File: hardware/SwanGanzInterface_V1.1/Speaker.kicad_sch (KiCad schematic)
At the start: 0 parts

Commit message: Added crystal loading caps
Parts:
- added C28: C, symbol Device:C
- added U15: OPA2350, Package_DIP:DIP-8_W7.62mm, symbol SGI_SymbolLib:OPA2350PA
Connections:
- new net: U15.1, U15.2 (-)
- new net +3V3: C28.1, U15.8 (V+)
- new net GND: C28.2, U15.4 (V-)

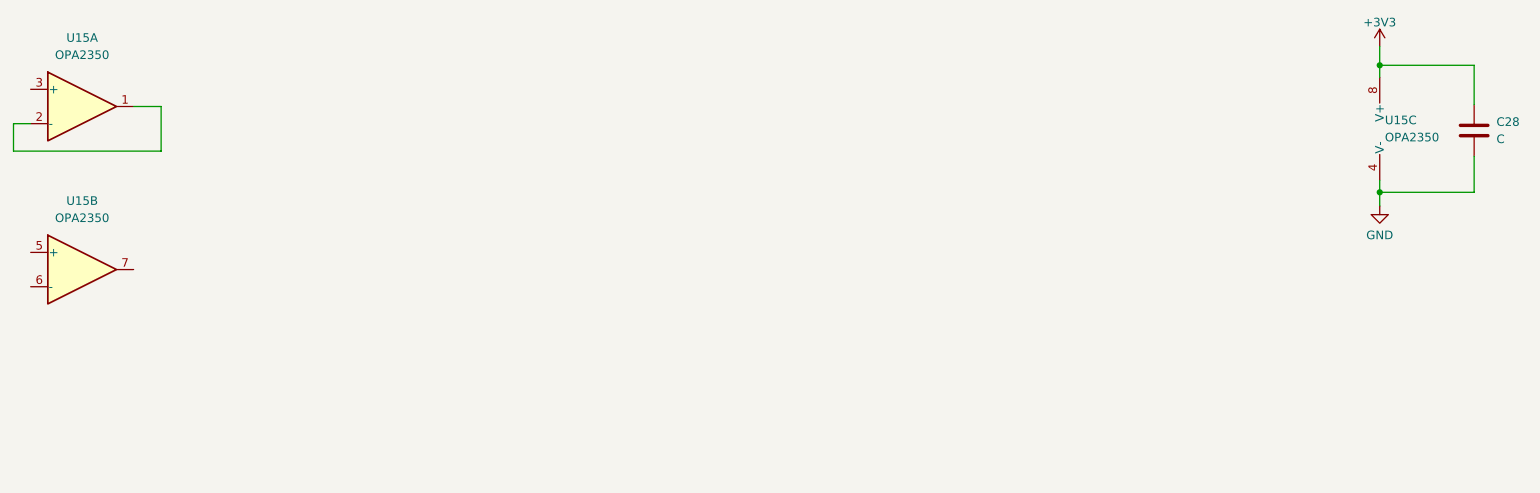
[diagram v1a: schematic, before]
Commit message: Added audio ampliier to symbol lib, began converting speaker circuit to audio amplifier
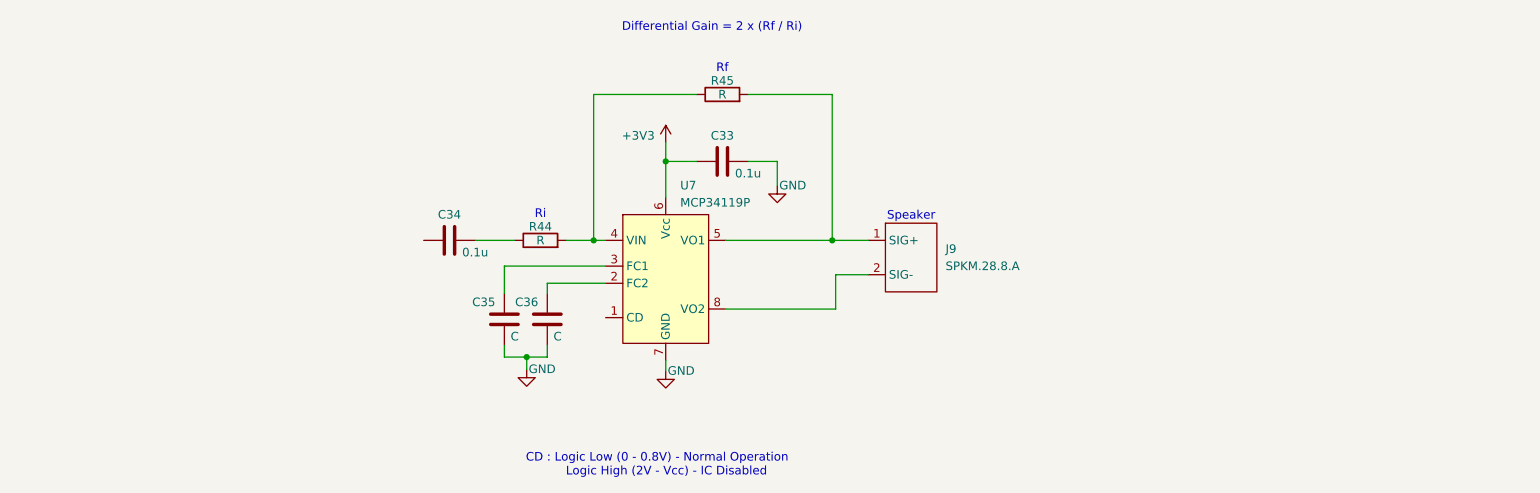
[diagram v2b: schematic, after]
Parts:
- removed C28: C, symbol Device:C
- removed U15: OPA2350, Package_DIP:DIP-8_W7.62mm, symbol SGI_SymbolLib:OPA2350PA
- added C33, C34: 0.1u, symbol Device:C
- added C35, C36: C, symbol Device:C
- added J9: SPKM.28.8.A, TerminalBlock:TerminalBlock_MaiXu_MX126-5.0-02P_1x02_P5.00mm, symbol SGI_SymbolLib:SPKM.28.8.A
- added R44, R45: R, symbol Device:R
- added U7: MCP34119P, Package_DIP:DIP-8_W7.62mm_LongPads, symbol SGI_SymbolLib:MCP34119P
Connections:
- net +3V3: now also C33.1, U7.6 (Vcc)
- net GND: now also C33.2, C35.1, C36.1, U7.7 (GND)
- new net: C34.2, R44.1
- new net: R44.2, R45.1, U7.4 (VIN)
- new net: C36.2, U7.2 (FC2)
- new net: J9.1 (SIG+), R45.2, U7.5 (VO1)
- new net: J9.2 (SIG-), U7.8 (VO2)
- new net: C35.2, U7.3 (FC1)
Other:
- note added: "CD : Logic Low (0 - 0.8V) - Normal Operation Logic High (2V - Vcc) - IC Disabled"
- note added: "Differential Gain = 2 x (Rf / Ri)"
- note added: "Rf"
- note added: "Ri"
- note added: "Speaker"

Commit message: Calculated speaker gain
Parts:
- R44: value R -> 16.6k
- R45: value R -> 10k
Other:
- note added: "DAC Range : 0 to 3.3V Gain = 1 / 3.3 = ~0.3 Differential Gain = 2 x (Rf / Ri) 0.3 = 2 x (Rf / Ri) 0.6 = Rf / Ri Ri = Rf / 0.6 Let Rf = 10 kOhms Ri = 10k / 0.6 Ri = 16.67 kOhms Rf = 10k kOhms Ri = 16.67 kOhms"
- note added: "P = V^2 / R 1W = V^2 / 8 V^2 = 8 V = 2.83 Vrms 2.83 Vrms = Vpp / (2 * sqrt(2)) Vpp = 1V"
- note added: "Speaker: Input Impedance : 8 Ohms Frequency Range : 100 Hz - 10kHz Nominal Power Input : 1 Watt RMS Maximum Power Input : 1.5 Watts"
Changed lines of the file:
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@@
+		)
+	)
+	(text "P = V^2 / R\n1W = V^2 / 8\nV^2 = 8\nV = 2.83 Vrms \n2.83 Vrms = Vpp / (2 * sqrt(2))\nVpp = 1V"
+		(exclude_from_sim no)
+		(at 227.33 64.77 0)
+		(effects
+			(font
+				(size 1.27 1.27)
+			)
+		)
+	)
+	(text "Speaker:\nInput Impedance : 8 Ohms\nFrequency Range : 100 Hz - 10kHz\nNominal Power Input : 1 Watt RMS\nMaximum Power Input : 1.5 Watts"
+		(exclude_from_sim no)
+		(at 226.568 46.228 0)
+		(effects
+			(font
+				(size 1.27 1.27)
+			)
 		)
 	)
@@
 		(exclude_from_sim no)
 		(at 188.976 48.006 0)
+		(effects
+			(font
+				(size 1.27 1.27)
+			)
+		)
+	)
+	(text "DAC Range : 0 to 3.3V \nGain = 1 / 3.3 = ~0.3\n\nDifferential Gain = 2 x (Rf / Ri) \n\n0.3 = 2 x (Rf / Ri)\n0.6 = Rf / Ri\nRi = Rf / 0.6\nLet Rf = 10 kOhms\nRi = 10k / 0.6\nRi = 16.67 kOhms\n\nRf = 10k kOhms\nRi = 16.67 kOhms\n\n"
+		(exclude_from_sim no)
+		(at 227.33 88.392 0)
 		(effects
 			(font
@@
 			)
 		)
-		(property "Value" "R"
+		(property "Value" "16.6k"
 			(at 134.112 51.562 90)
 			(effects
@@
 			)
 		)
-		(property "Value" "R"
+		(property "Value" "10k"
 			(at 161.036 29.972 90)
 			(effects

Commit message: Added lots, moving to 64 pin micro
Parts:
- C35: value C -> 1u
- C36: value C -> 5u
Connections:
- net SPEAK_CD: now reaches U7.1 (CD)
- net SPEAK_DAC: now reaches C34.1
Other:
- moved on the sheet: C33, C34, C35, C36, J9, R44, R45, U7

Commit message: Got 64 pin MSP symbol and footprint and started implementation
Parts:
- added C4: 0.1u, Capacitor_SMD:C_0603_1608Metric, symbol Device:C
- added U5: AdaFruit_1590, SGI_FootprintsLib:AdaFruit_1590, symbol SGI_SymbolLib:ADAFRUIT_1590_RA8875
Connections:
- net +3V3: now also C4.1, U5.1 (VIN)
- net GND: now also C4.2, U5.2 (GND)
- net SPEAK_CD renamed SPEAK_CD_PA14
- new net LCD_CS_PB6: U5.8 (CS)
- new net LCD_INT_PB10: U5.11 (INT)
- new net LCD_LITE_PB13: U5.4 (LITE)
- new net LCD_PICO_PB8: U5.7 (MOSI)
- new net LCD_POCI_PB7: U5.6 (MISO)
- new net LCD_RST_PB12: U5.9 (RST)
- new net LCD_SCK_PB9: U5.5 (SCK)
- new net LCD_WAIT_PB11: U5.10 (WAIT)
- new net LCD_X+: U5.15 (X+)
- new net LCD_X-: U5.14 (X-)
- new net LCD_Y+: U5.12 (Y+)
- new net LCD_Y-: U5.13 (Y-)
- no-connect marks 0 -> 1
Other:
- note added: "LCD Driver"

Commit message: Added debug pins to touch ic and ft232
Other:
- note added: "Add Debug Pins"
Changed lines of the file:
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@@
+		)
+	)
+	(text "Add Debug Pins"
+		(exclude_from_sim no)
+		(at 74.676 129.286 0)
+		(effects
+			(font
+				(size 1.27 1.27)
+			)
 		)
 	)

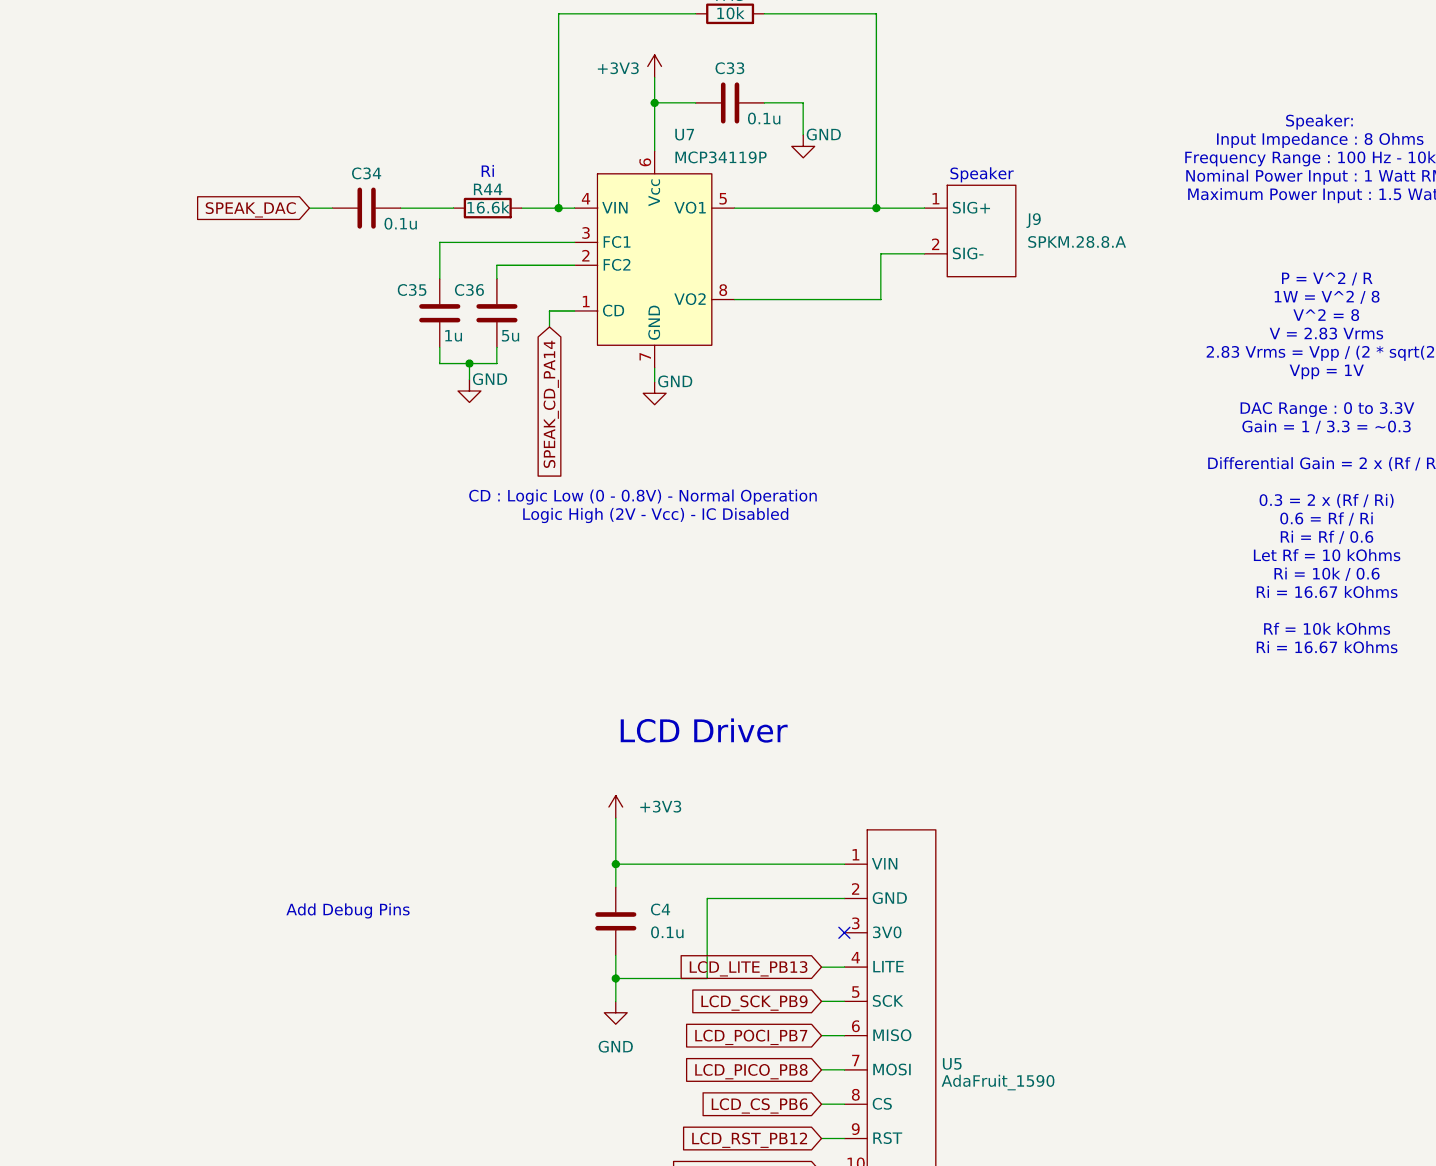
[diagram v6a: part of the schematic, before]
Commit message: LCD spi debugging pins
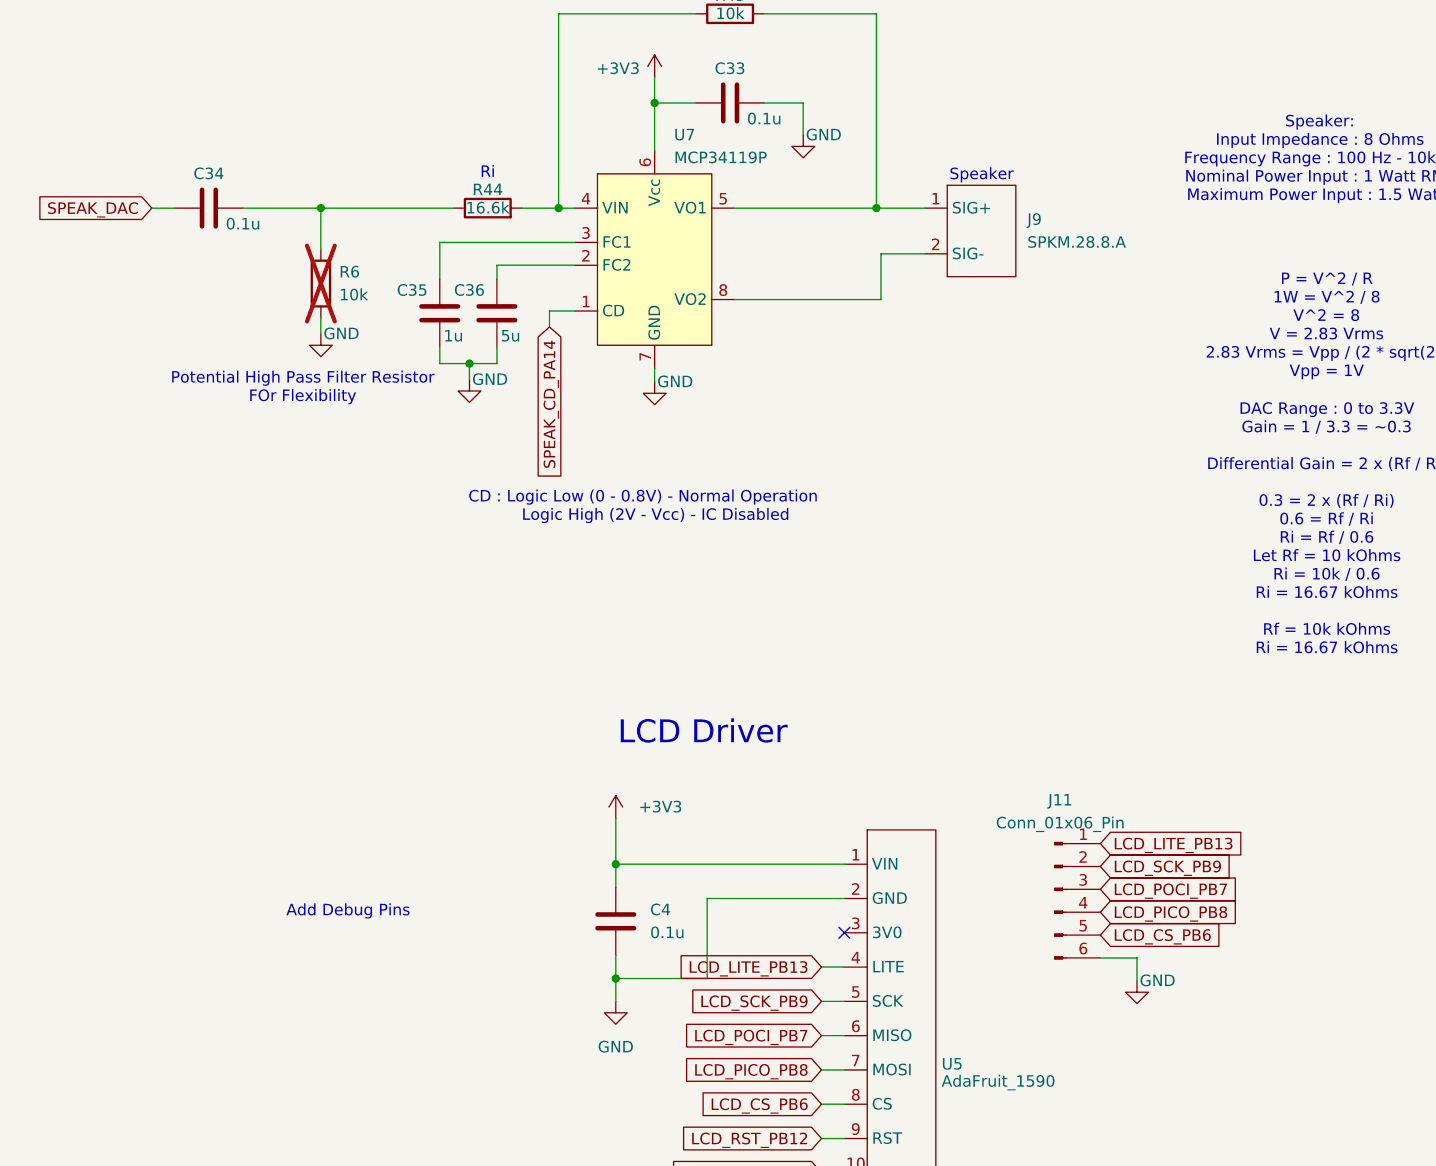
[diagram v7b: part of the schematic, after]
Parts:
- added J11: Conn_01x06_Pin, symbol Connector:Conn_01x06_Pin
- added R6: 10k, symbol Device:R
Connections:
- net GND: now also J11.6 (Pin_6), R6.2
- net LCD_CS_PB6: now also J11.5 (Pin_5)
- net LCD_LITE_PB13: now also J11.1 (Pin_1)
- net LCD_PICO_PB8: now also J11.4 (Pin_4)
- net LCD_POCI_PB7: now also J11.3 (Pin_3)
- net LCD_SCK_PB9: now also J11.2 (Pin_2)
- net at C34.2, R44.1: now also R6.1
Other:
- note added: "Potential High Pass Filter Resistor FOr Flexibility"
- moved on the sheet: C34

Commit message: Schematic Check
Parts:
- renumbered C34 to C32, C35 to C33, C36 to C34, C4 to C35, C33 to C36, J9 to J12, J11 to J13, R6 to R46, R44 to R47, R45 to R48, U7 to U12, U5 to U13
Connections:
- net SPEAK_DAC renamed SPEAK_DAC_PA15
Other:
- note added: "3V0 is a voltage output from an LDO on the driver board"
- note added: "Audio Amplifier"
- note added: "Audio Amplifier and LCD Driver"
- note added: "LITE is a PWM input for brightness"
- note added: "Screw Terminal Connection for Speaker"
- note removed: "Add Debug Pins"
- moved on the sheet: C32, C33, C34, C35, C36, J12, J13, R46, R47, R48, U12
